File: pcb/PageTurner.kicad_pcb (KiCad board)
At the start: 2 copper layers, 30 x 20 mm, 19 parts, among them J1 AudioJack2, J2 AudioJack2, J3 USB_C_Receptacle, J5 TC2030_SWD, SW1 RST, SW2 BOOT, U1 STM32F042F6Px, U2 TPS7A0533PDBV

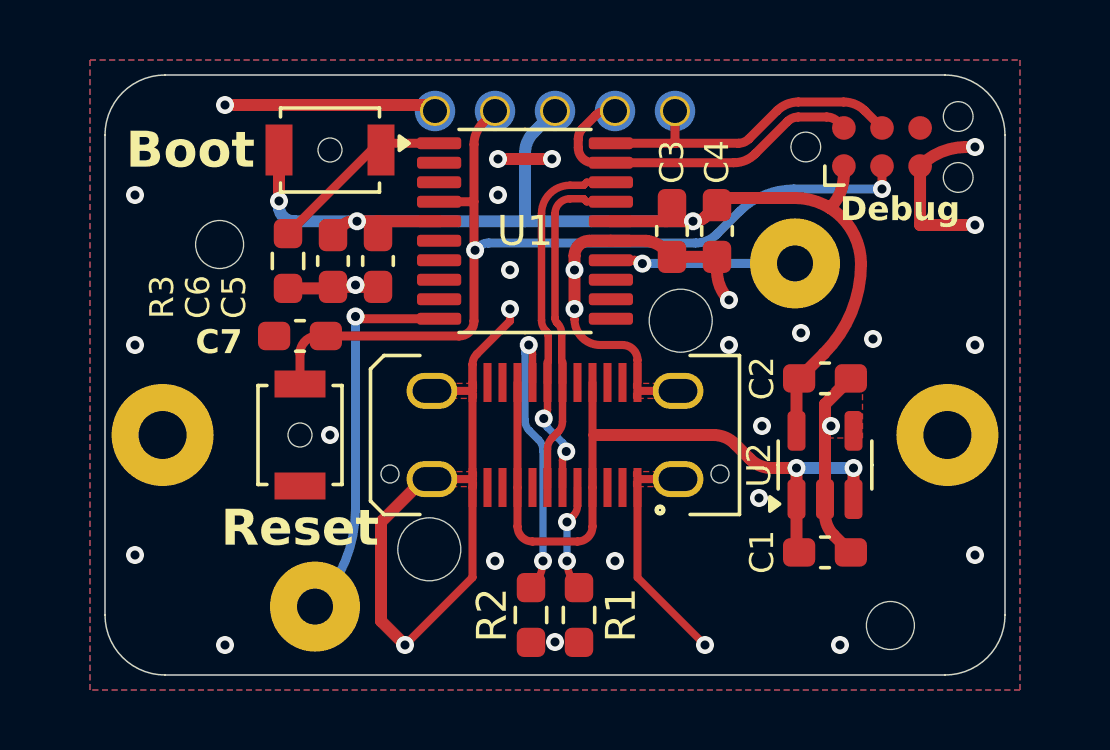
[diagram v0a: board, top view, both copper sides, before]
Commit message: Increase spacing between jacks slightly
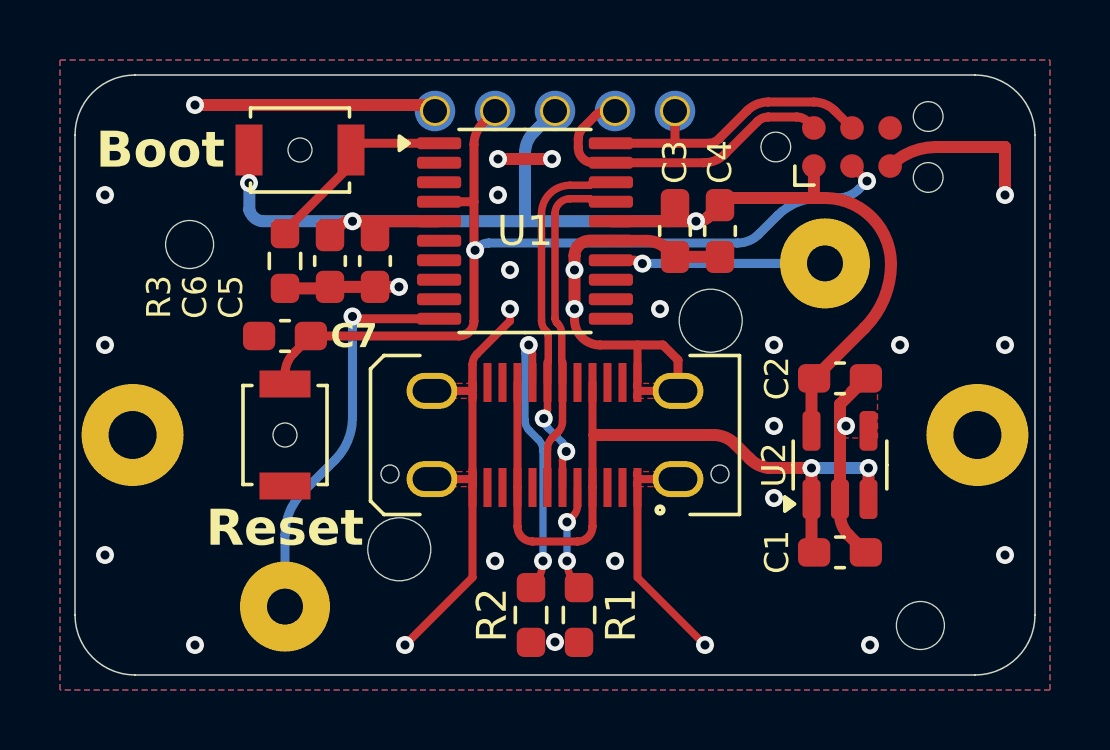
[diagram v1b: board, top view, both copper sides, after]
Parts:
- moved J1 1.00 mm to (91.0, 105.7)
- moved J2 1.00 mm to (109.0, 94.3)
- moved J5 1.00 mm to (109.9, 90.4)
- moved SW2 1.00 mm to (91.5, 90.5)
- moved C1 0.50 mm to (109.5, 103.9)
- moved C2 0.50 mm to (109.5, 98.1)
- moved C7 0.50 mm to (91.0, 96.7)
- moved SW1 0.50 mm to (91.0, 100.0)
- moved U2 0.50 mm to (109.5, 101.0)
- moved C3 0.10 mm to (104.0, 93.2)
- moved C4 0.10 mm to (105.5, 93.2)
- moved C5 0.10 mm to (94.0, 94.2)
- moved C6 0.10 mm to (92.5, 94.2)
- moved R3 0.10 mm to (91.0, 94.2)
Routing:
- net GND: track 67.1 -> 63.1 mm, vias 31 -> 28
- net +3V3: track 42.3 -> 43.8 mm
- net SWDIO: track 10.9 -> 9.59 mm
- net SWCLK: track 10.9 -> 9.92 mm
- net SW1: track 14.1 -> 13.2 mm
- net D+: track 12.5 -> 11.8 mm
- net D-: track 11.6 -> 10.9 mm
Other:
- board size 30 x 20 mm -> 32 x 20 mm
- board text removed: "Debug"

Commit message: Update bom, fix decoupling capacitor value
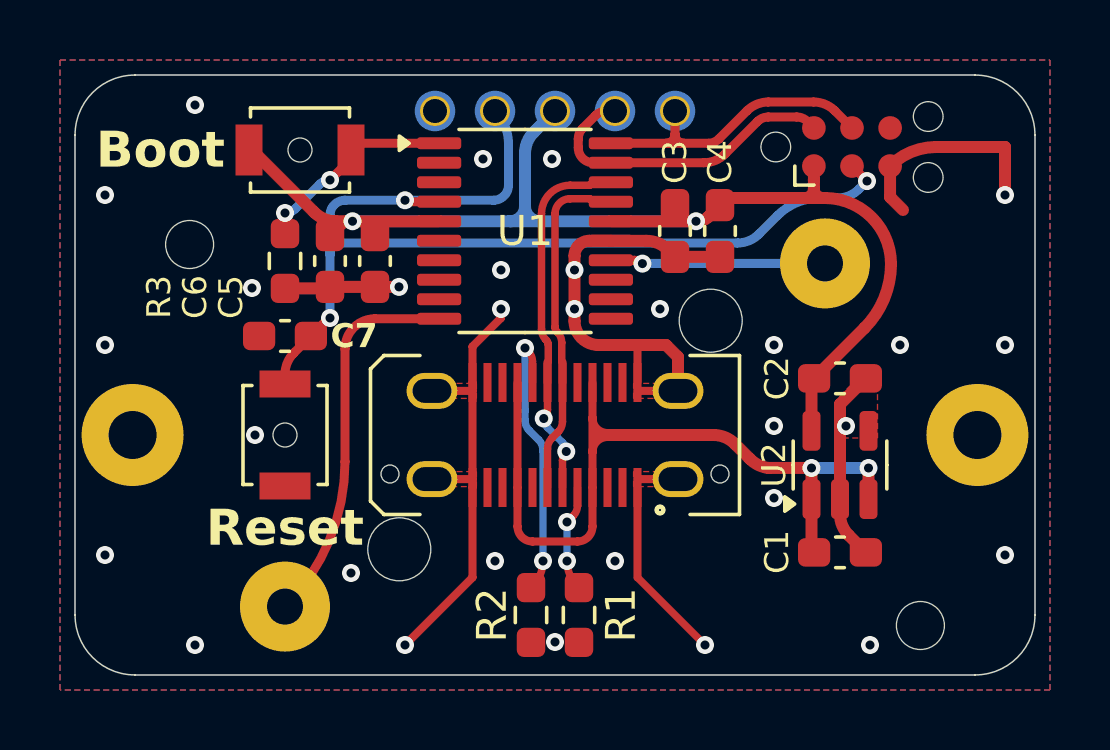
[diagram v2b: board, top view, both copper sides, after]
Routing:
- net GND: track 63.1 -> 55.1 mm, vias 28 -> 30
- net RST: track 30.5 -> 36.3 mm, vias 2 -> 3
- net VBUS: track 25.9 -> 27.4 mm
- net SWCLK: track 9.92 -> 10.5 mm
- net SW1: track 13.2 -> 12.8 mm, vias 1 -> 0
- net BOOT0: track 5.82 -> 5.61 mm, vias 0 -> 2
- net +3V3: track 43.8 -> 43.9 mm, vias 3 -> 2

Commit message: Add ESD diodes for pedal inputs
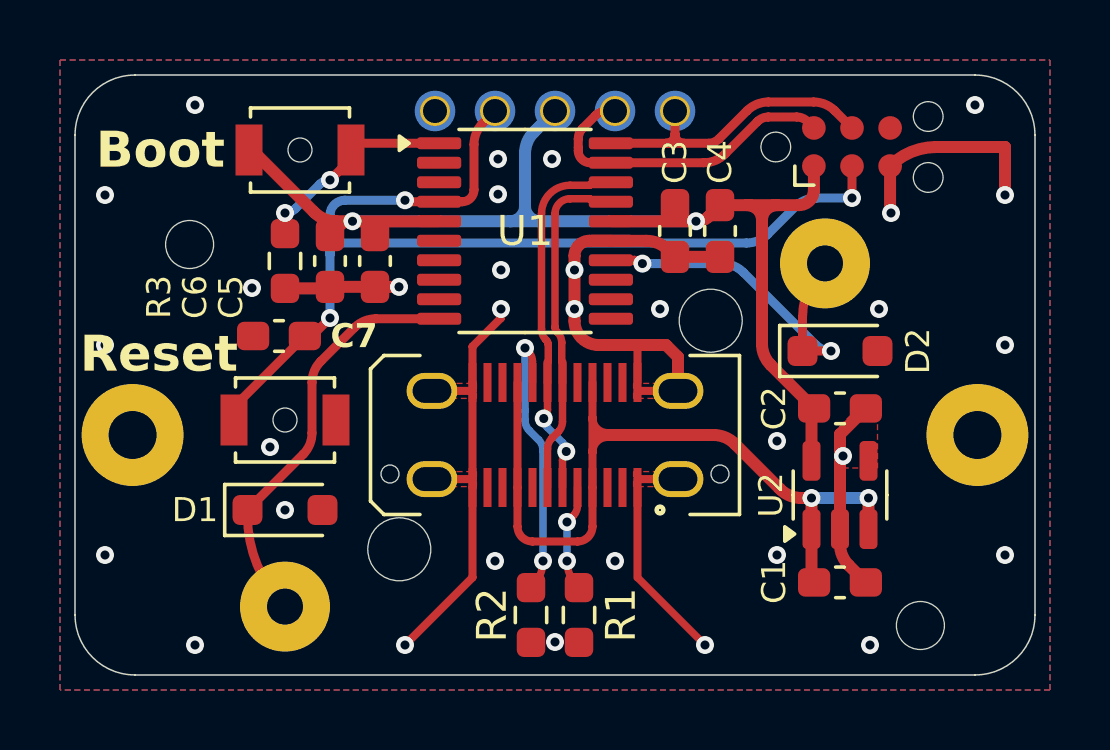
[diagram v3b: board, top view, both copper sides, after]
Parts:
- added D1: PESD3V3L1BA, Diode_SMD:D_SOD-323_HandSoldering, F.Cu at (91.0, 102.5)
- added D2: PESD3V3L1BA, Diode_SMD:D_SOD-323_HandSoldering, F.Cu at (109.5, 97.2)
- C4: value 47u -> 4.7u
- moved C1 1.00 mm to (109.5, 104.9)
- moved C2 1.00 mm to (109.5, 99.1)
- moved U2 1.00 mm to (109.5, 102.0)
- moved SW1 0.50 mm to (91.0, 99.5), turned to 0 degrees
- moved C7 0.20 mm to (90.8, 96.7)
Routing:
- net SW2: track 6.17 -> 12.6 mm, vias 1 -> 2
- net SW1: track 12.8 -> 13.9 mm
- net SWDIO: track 9.59 -> 10.2 mm
- net +3V3: track 43.9 -> 43.3 mm
- net GND: vias 30 -> 32

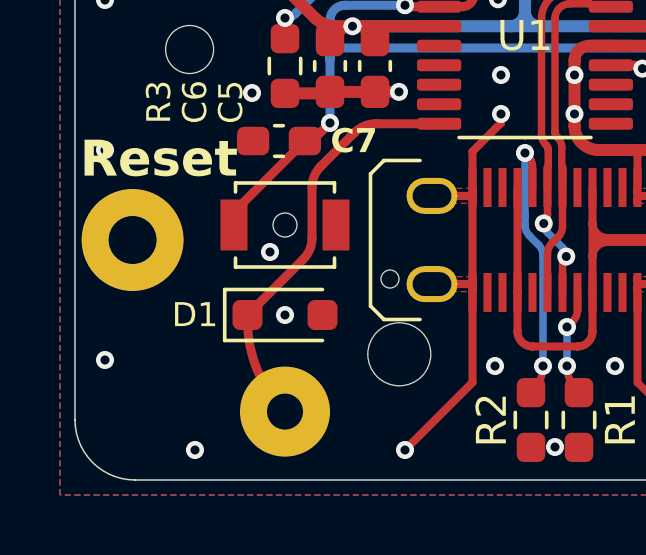
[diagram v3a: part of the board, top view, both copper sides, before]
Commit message: Use cheaper ESD diode
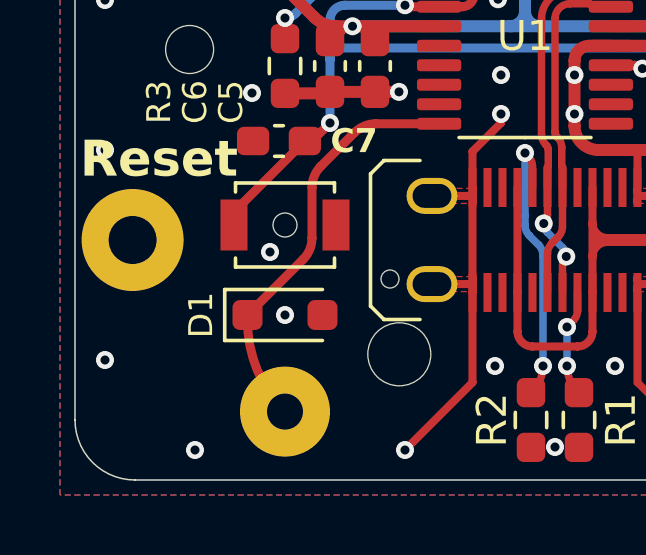
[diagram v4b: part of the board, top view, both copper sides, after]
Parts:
- D1, D2: value PESD3V3L1BA -> SD03C-7
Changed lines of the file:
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@@
 		(tags "capacitor handsolder")
 		(property "Reference" "C7"
-			(at -2.5 0 0)
+			(at -2.5 0 180)
 			(layer "F.SilkS")
 			(effects
@@
 		(layer "F.Cu")
 		(at 109.5 102 90)
-		(descr "SOT, 5 Pin (~), generated with kicad-footprint-generator ipc_gullwing_generator.py")
+		(descr "SOT, 5 Pin (JEDEC MO-178 Var AA https://www.jedec.org/document_search?search_api_views_fulltext=MO-178), generated with kicad-footprint-generator ipc_gullwing_generator.py")
 		(tags "SOT TO_SOT_SMD")
 		(property "Reference" "U2"
@@
 			)
 		)
-		(property "Value" "PESD3V3L1BA"
+		(property "Value" "SD03C-7"
 			(at 0.1 1.9 360)
 			(layer "F.Fab")
@@
 			)
 		)
-		(property "Datasheet" ""
+		(property "Datasheet" "https://www.diodes.com/assets/Datasheets/SD03C.pdf"
 			(at 0 0 0)
 			(unlocked yes)
@@
 		(tags "SOD-323")
 		(property "Reference" "D1"
-			(at -3 0 0)
+			(at -2.8 0 90)
 			(layer "F.SilkS")
 			(effects
@@
 			)
 		)
-		(property "Value" "PESD3V3L1BA"
+		(property "Value" "SD03C-7"
 			(at 0.1 1.9 0)
 			(layer "F.Fab")
@@
 			)
 		)
-		(property "Datasheet" ""
+		(property "Datasheet" "https://www.diodes.com/assets/Datasheets/SD03C.pdf"
 			(at 0 0 0)
 			(unlocked yes)
